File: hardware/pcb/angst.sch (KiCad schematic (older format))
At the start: 1 part

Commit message: Finish work on MCU block, start work on driver block
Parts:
- removed U?: STM32F303RBTx, Package_QFP:LQFP-64_10x10mm_P0.5mm, symbol MCU_ST_STM32F3:STM32F303RBTx
- added C? (x7): 100n, symbol Device:C_Small
- added D?: LED, symbol Device:LED
- added L?: INDUCTOR, symbol pspice:INDUCTOR
- added R?: 100k, symbol Device:R
- added R? (x3): 4k7, symbol Device:R
- added R?: 10k, symbol Device:R
- added R?: 22, symbol Device:R
- added R?: 560, symbol Device:R
- added SW?: SW_Push, symbol Switch:SW_Push
- added U?: STM32F303RETx, Package_QFP:LQFP-64_10x10mm_P0.5mm, symbol MCU_ST_STM32F3:STM32F303RETx
- added U?: M24C02-RDW, Package_SO:TSSOP-8_4.4x3mm_P0.65mm, symbol Memory_EEPROM:M24C02-RDW
- added Y?: Crystal_GND24, symbol Device:Crystal_GND24
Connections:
- net labels added: +3V3, GND, GNDA, PA0, PA1, PA10, PA11, PA12, PA13, PA14, PA15, PA2, PA3, PA4, PA5, PA6, PA7, PA8, PA9, PB0, PB1, PB10, PB11, PB12, PB13, PB14, PB2, PB3, PB4, PB5, PB6, PB7, PB8, PB9, PC0, PC1, PC10, PC11, PC12, PC13, PC14, PC15, PC2, PC3, PC4, PC5, PC7, PC8, PC9, PD2, nRST, pC6
- wire segments 0 -> 140
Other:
- note added: "EEPROM"
- note added: "uC - STM32F303"

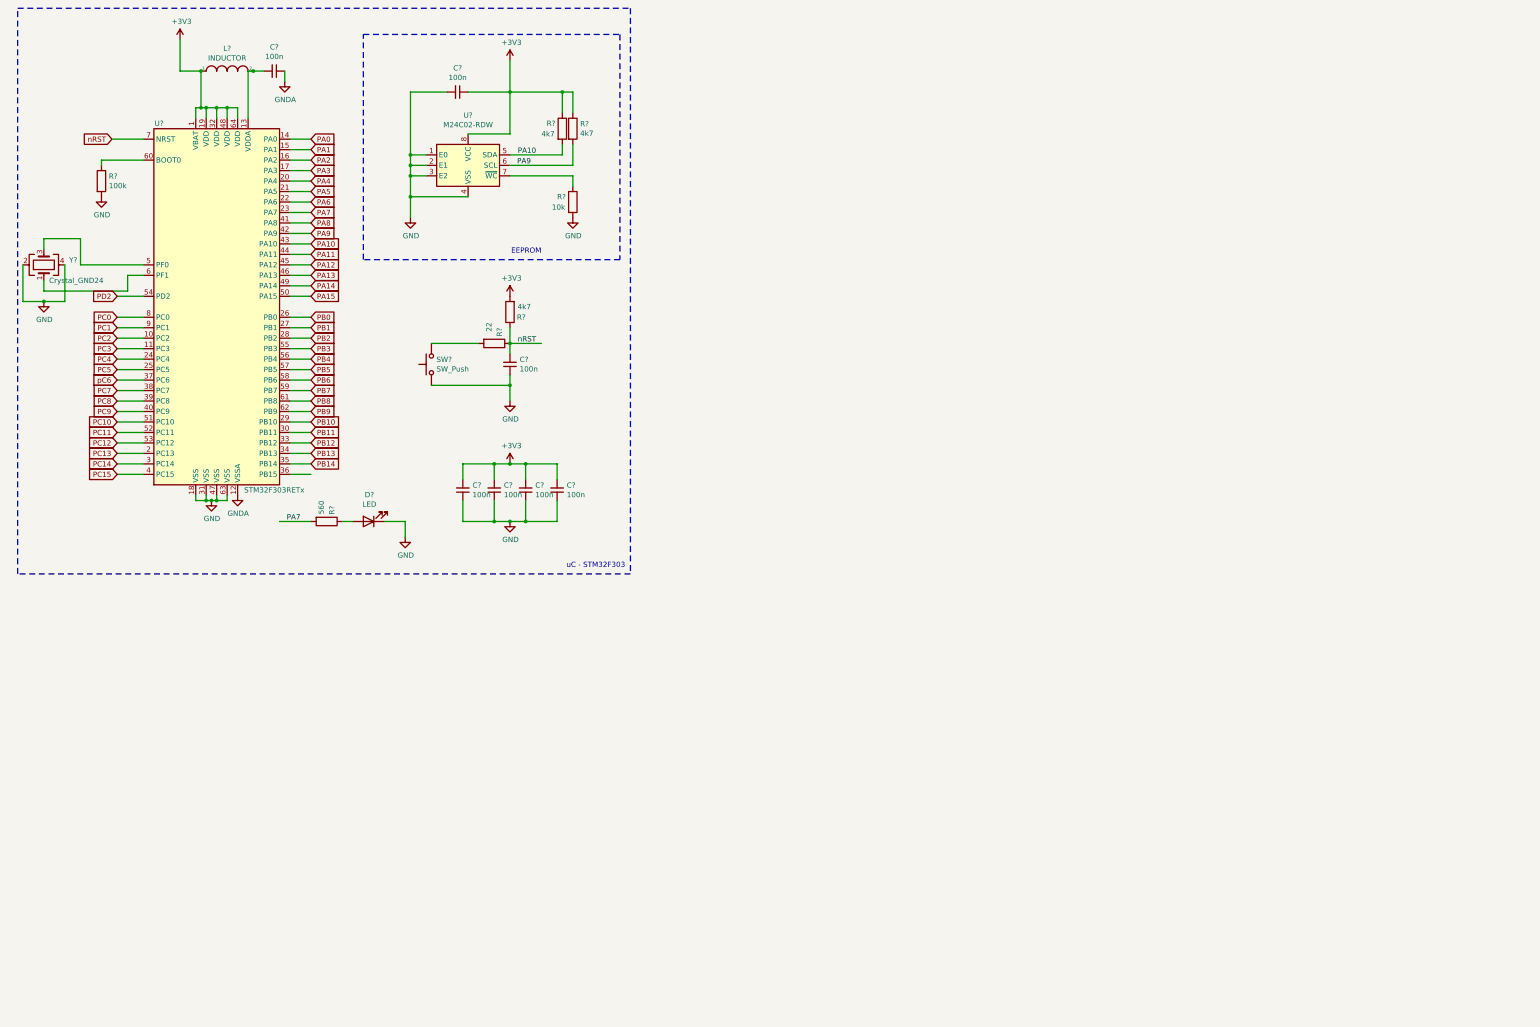
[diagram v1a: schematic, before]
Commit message: Add motor driver block and connector block.
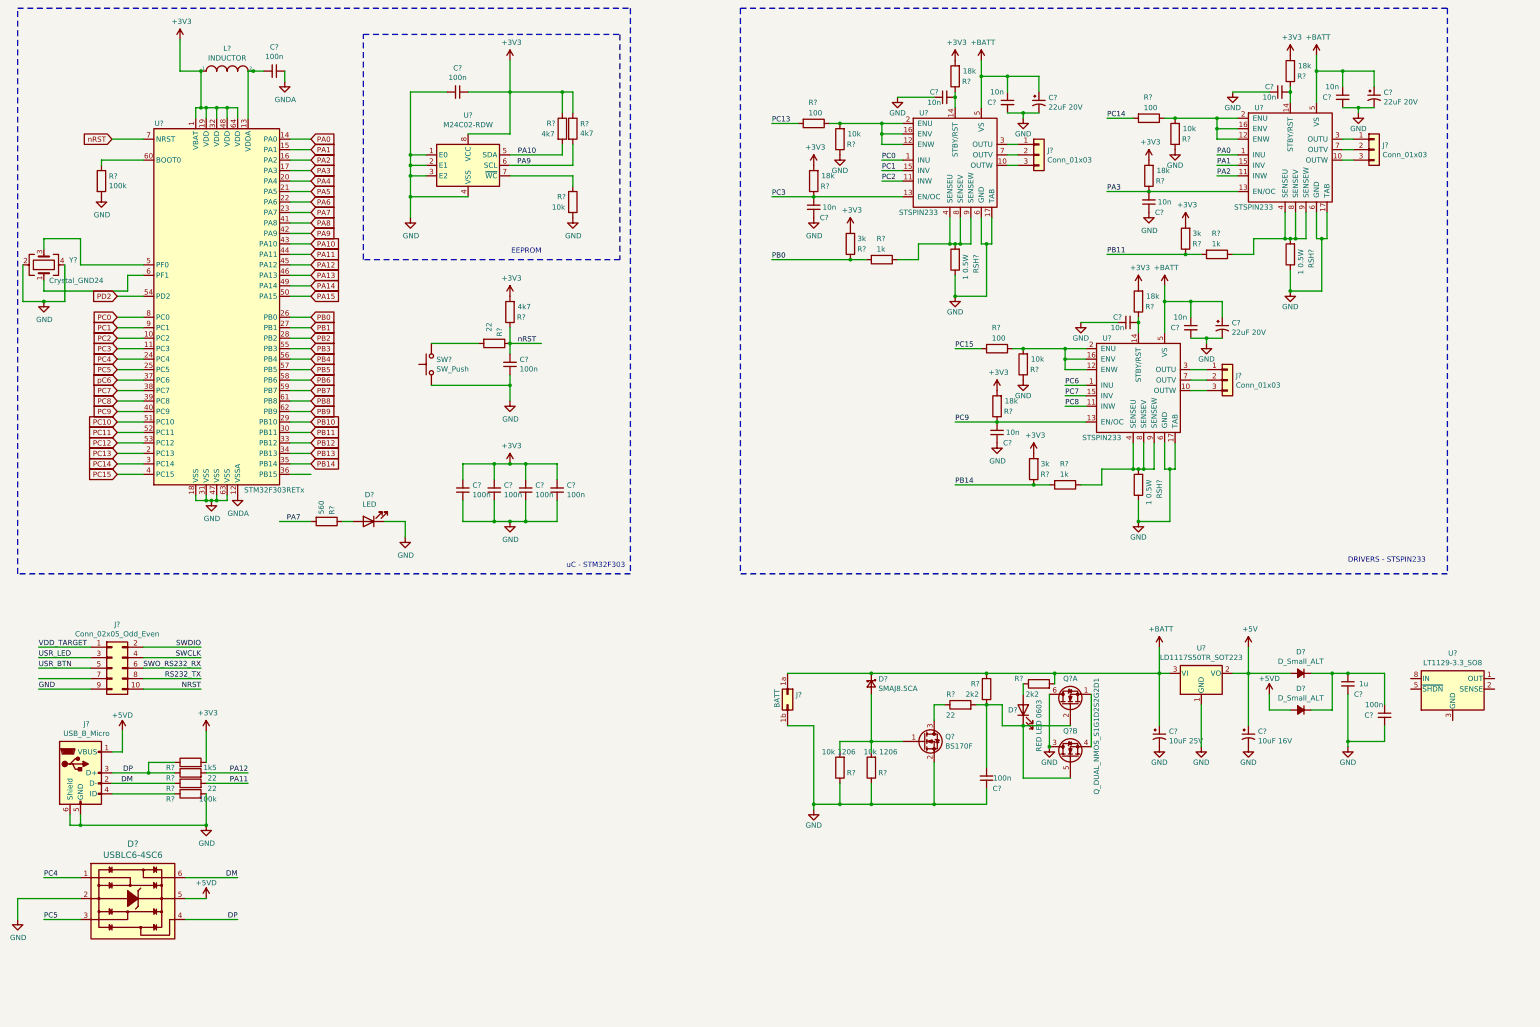
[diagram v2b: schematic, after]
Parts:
- added C? (x9): 10n, symbol Device:C_Small
- added C? (x3): 22uF 20V, symbol Device:CP1_Small
- added C? (x2): 100n, symbol Device:C_Small
- added C?: 10uF 25V, symbol Device:CP1_Small
- added C?: 10uF 16V, symbol Device:CP1_Small
- added C?: 1u, symbol Device:C_Small
- added D?: SMAJ8.5CA, symbol Device:D_Schottky_Small
- added D?: RED LED 0603, symbol Device:LED
- added D? (x2): D_Small_ALT, symbol Device:D_Small_ALT
- added D?: USBLC6-4SC6, digikey-footprints:SOT23-6L, symbol dk_TVS-Diodes:USBLC6-4SC6
- added J? (x3): Conn_01x03, symbol Connector_Generic:Conn_01x03
- added J?: Conn_02x05_Odd_Even, symbol Connector_Generic:Conn_02x05_Odd_Even
- added J?: BATT, symbol Connector_Generic:Conn_02x01_Row_Letter_Last
- added J?: USB_B_Micro, symbol Connector:USB_B_Micro
- added Q?: BS170F, Package_TO_SOT_SMD:SOT-23, symbol Transistor_FET:BS170F
- added Q? (x2): Q_DUAL_NMOS_S1G1D2S2G2D1, symbol Device:Q_DUAL_NMOS_S1G1D2S2G2D1
- added R? (x3): 100, symbol Device:R
- added R? (x3): 10k, symbol Device:R
- added R? (x6): 18k, symbol Device:R
- added R? (x3): 1k, symbol Device:R
- added R? (x3): 3k, symbol Device:R
- added R? (x2): 10k 1206, Resistor_SMD:R_1206_3216Metric_Pad1.42x1.75mm_HandSolder, symbol Device:R
- added R? (x3): 22, symbol Device:R
- added R? (x2): 2k2, symbol Device:R
- added R?: 100k, symbol Device:R
- added R?: 1k5, symbol Device:R
- added RSH? (x3): 1 0.5W, symbol Device:R
- added U? (x3): STSPIN233, symbol angst:STSPIN233
- added U?: LD1117S50TR_SOT223, Package_TO_SOT_SMD:SOT-223-3_TabPin2, symbol Regulator_Linear:LD1117S50TR_SOT223
- added U?: LT1129-3.3_SO8, Package_SO:SOIC-8_3.9x4.9mm_P1.27mm, symbol Regulator_Linear:LT1129-3.3_SO8
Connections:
- net +3V3: now also R?.2, R?.2, R?.2, R?.2, R?.2, R?.2, R?.2, R?.2, R?.2, R?.2
- net GND: now also C?.1, C?.1, C?.1, C?.1, C?.1, C?.1, C?.1, C?.2, C?.2, C?.2, C?.2, C?.2, C?.2, C?.2, C?.2, C?.2, C?.2, D?.2, J?.1b (Pin_1b), J?.5 (GND), J?.6 (Shield), J?.9 (Pin_9), Q?.2 (S), Q?.3 (D), Q?.6 (D), R?.1, R?.1, R?.1, R?.1, R?.1, R?.2, RSH?.1, RSH?.1, RSH?.1, U?.1 (GND), U?.17 (TAB), U?.17 (TAB), U?.17 (TAB), U?.6 (GND), U?.6 (GND), U?.6 (GND)
- net PA0: now also U?.1 (INU)
- net PA1: now also U?.15 (INV)
- net PA11: now also R?.2
- net PA12: now also R?.2
- net PA2: now also U?.11 (INW)
- net PA3: now also C?.2, R?.1, U?.13 (EN/OC)
- net PB0: now also R?.1, R?.2
- net PB11: now also R?.1, R?.2
- net PB14: now also R?.1, R?.2
- net PC0: now also U?.1 (INU)
- net PC1: now also U?.15 (INV)
- net PC13: now also R?.2
- net PC14: now also R?.2
- net PC15: now also R?.2
- net PC2: now also U?.11 (INW)
- net PC3: now also C?.2, R?.1, U?.13 (EN/OC)
- net PC4: now also D?.1
- net PC5: now also D?.3
- net PC7: now also U?.15 (INV)
- net PC8: now also U?.11 (INW)
- net PC9: now also C?.2, R?.1, U?.13 (EN/OC)
- new net: J?.3 (Pin_3), U?.10 (OUTW) (x3)
- new net: R?.1, R?.2, U?.12 (ENW), U?.16 (ENV), U?.2 (ENU) (x3)
- new net: C?.2, R?.1, U?.14 (STBY/RST) (x3)
- new net: J?.1 (Pin_1), U?.3 (OUTU) (x3)
- new net: R?.1, RSH?.2, U?.4 (SENSEU), U?.8 (SENSEV), U?.9 (SENSEW) (x3)
- new net: J?.2 (Pin_2), U?.7 (OUTV) (x3)
- new net: D?.2 (A), Q?.1 (G), R?.2, R?.2
- new net: Q?.3 (D), R?.1
- new net: C?.2, D?.1 (K), Q?.2 (G), Q?.5 (G), R?.2, R?.2
- new net: Q?.1 (S), Q?.4 (S)
- new net: D?.2 (A), R?.1
- new net: C?.1, C?.1, D?.1 (K), D?.1 (K)
- new net: U?.3 (GND), U?.6 (GND), U?.7 (GND)
- new net: J?.4 (ID), R?.1
- new net +5V: C?.1, D?.2 (A), U?.2 (VO)
- new net +5VD: D?.2 (A), D?.5, J?.1 (VBUS)
- new net +BATT: C?.1, C?.1, C?.1, C?.1, C?.1, C?.1, C?.1, D?.1 (K), J?.1a (Pin_1a), R?.1, R?.2, U?.3 (VI), U?.5 (VS), U?.5 (VS), U?.5 (VS)
- new net DM: D?.6, J?.2 (D-), R?.1
- new net DP: D?.4, J?.3 (D+), R?.1, R?.1
- new net NRST: J?.10 (Pin_10)
- new net PC6: U?.1 (INU)
- new net RS232_TX: J?.8 (Pin_8)
- new net SWCLK: J?.4 (Pin_4)
- new net SWDIO: J?.2 (Pin_2)
- new net SWO_RS232_RX: J?.6 (Pin_6)
- new net USR_BTN: J?.5 (Pin_5)
- new net USR_LED: J?.3 (Pin_3)
- new net VDD_TARGET: J?.1 (Pin_1)
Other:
- note added: "DRIVERS - STSPIN233\n"

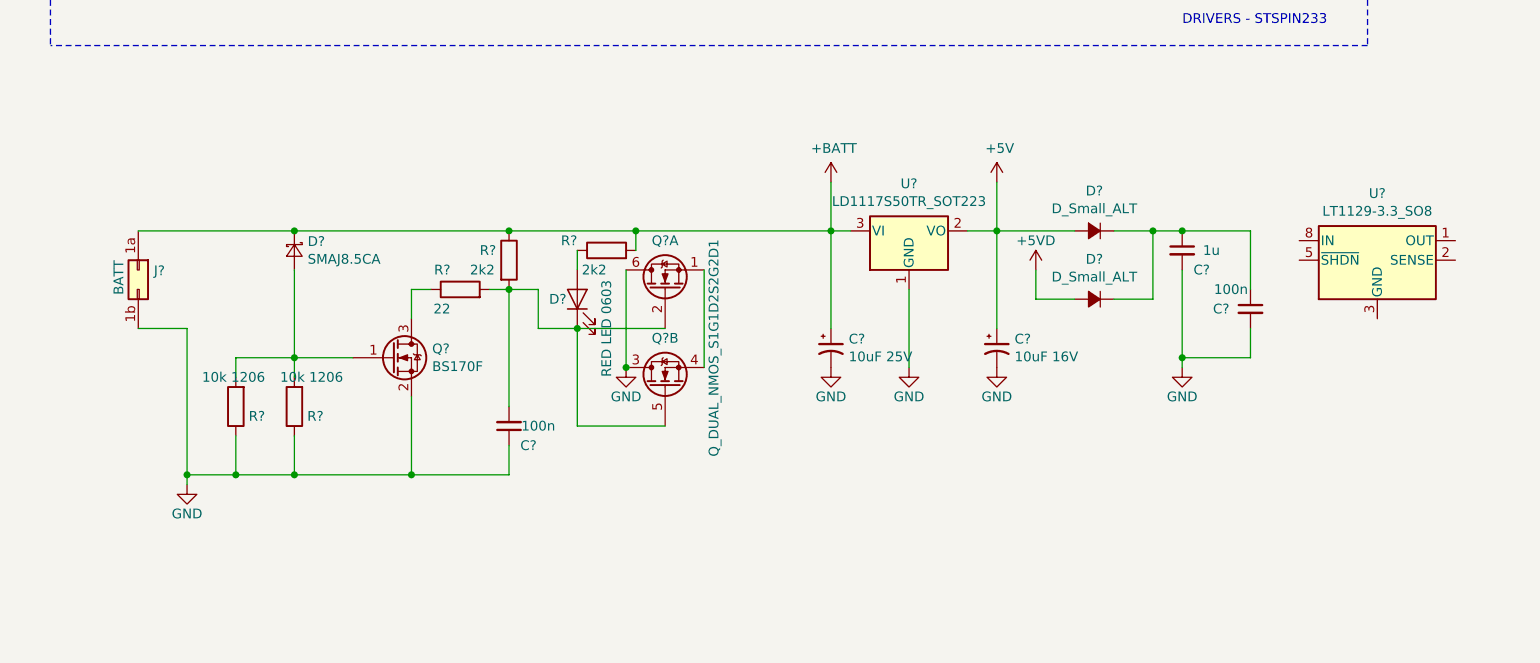
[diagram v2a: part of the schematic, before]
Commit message: Add power block
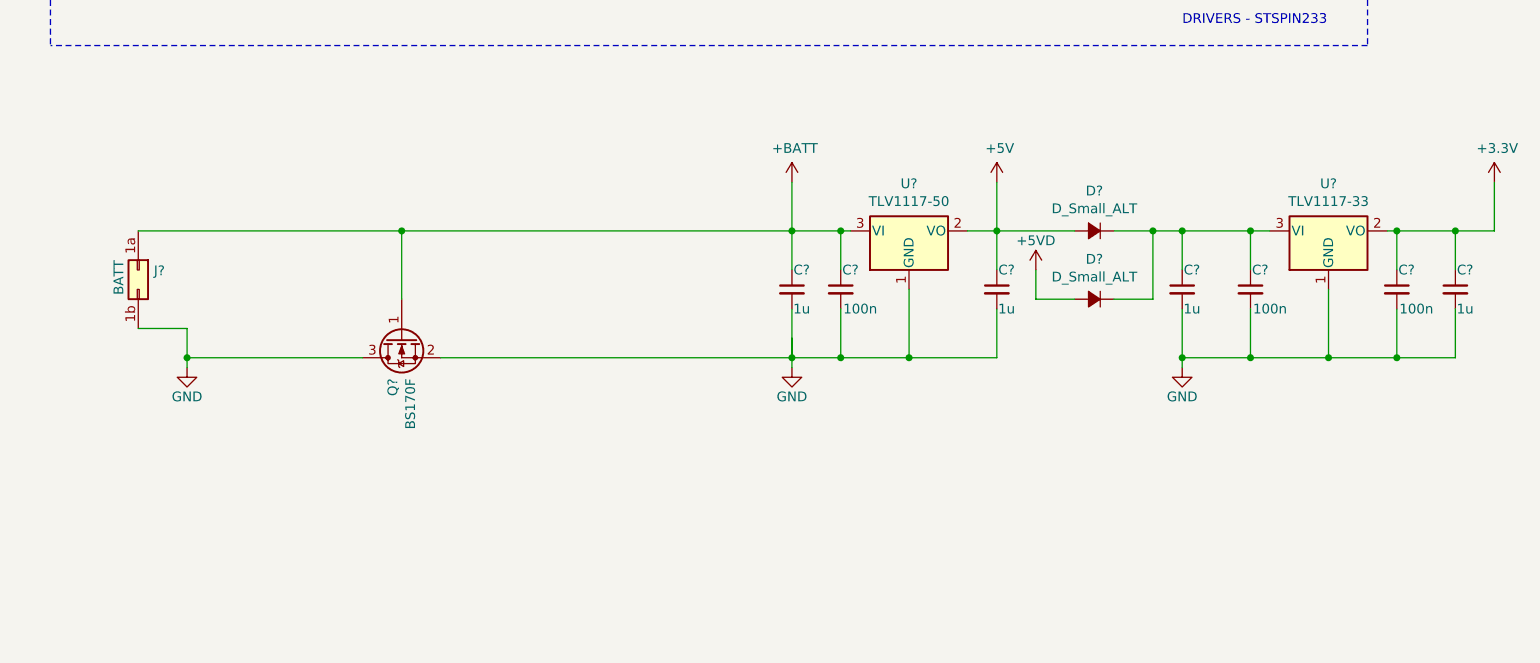
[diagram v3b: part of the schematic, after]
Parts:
- removed C?: 100n, symbol Device:C_Small
- removed C?: 10uF 25V, symbol Device:CP1_Small
- removed C?: 10uF 16V, symbol Device:CP1_Small
- removed D?: SMAJ8.5CA, symbol Device:D_Schottky_Small
- removed D?: RED LED 0603, symbol Device:LED
- removed Q? (x2): Q_DUAL_NMOS_S1G1D2S2G2D1, symbol Device:Q_DUAL_NMOS_S1G1D2S2G2D1
- removed R? (x2): 10k 1206, Resistor_SMD:R_1206_3216Metric_Pad1.42x1.75mm_HandSolder, symbol Device:R
- removed R?: 22, symbol Device:R
- removed R? (x2): 2k2, symbol Device:R
- removed U?: LD1117S50TR_SOT223, Package_TO_SOT_SMD:SOT-223-3_TabPin2, symbol Regulator_Linear:LD1117S50TR_SOT223
- removed U?: LT1129-3.3_SO8, Package_SO:SOIC-8_3.9x4.9mm_P1.27mm, symbol Regulator_Linear:LT1129-3.3_SO8
- added C? (x3): 1u, symbol Device:C_Small
- added C? (x2): 100n, symbol Device:C_Small
- added U?: TLV1117-33, symbol Regulator_Linear:TLV1117-33
- added U?: TLV1117-50, symbol Regulator_Linear:TLV1117-50
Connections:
- net +3V3: now also C?.1, C?.1, U?.2 (VO)
- net +5V: now also C?.1, U?.2 (VO)
- net +BATT: now also Q?.1 (G), C?.1, C?.1, U?.3 (VI)
- net GND: now also Q?.3 (D), C?.2, C?.2, C?.2, C?.2, C?.2, U?.1 (GND), U?.1 (GND)
- net at C?.1, C?.1, D?.1 (K)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: now also U?.3 (VI)
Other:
- moved on the sheet: C?, Q?

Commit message: Clean up power concept. Add connector block
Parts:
- removed D?: D_Small_ALT, symbol Device:D_Small_ALT
- removed Q?: BS170F, Package_TO_SOT_SMD:SOT-23, symbol Transistor_FET:BS170F
- added D3: SMAJ8.5CALFCT-ND, Diode_SMD:D_SMA, symbol Device:D_ALT
- added D4: STPS2L30, Diode_SMD:D_SMA, symbol Device:D_Small_ALT
- added J? (x2): Conn_01x02_Male, symbol Connector:Conn_01x02_Male
- added J?: Conn_01x04_Male, symbol Connector:Conn_01x04_Male
- added Q1: IRLML6401TRPBF, digikey-footprints:SOT-23-3, symbol dk_Transistors-FETs-MOSFETs-Single:IRLML6401TRPBF
- added R22: 2k2, Resistor_SMD:R_0603_1608Metric_Pad1.05x0.95mm_HandSolder, symbol Device:R
- added R? (x2): 47k, Resistor_SMD:R_0603_1608Metric_Pad1.05x0.95mm_HandSolder, symbol Device:R
- C1, C10, C11, C13, C14, C15, C16, C17, C19, C2, C20, C21, C22, C24, C25, C26, C3, C4, C5, C6, C7, C8, C9: renamed from C?; footprint (none) -> Capacitor_SMD:C_0603_1608Metric_Pad1.05x0.95mm_HandSolder
- C12, C18, C23: renamed from C?; footprint (none) -> Capacitor_Tantalum_SMD:CP_EIA-1608-08_AVX-J_Pad1.25x1.05mm_HandSolder
- D2: renamed from D?; footprint (none) -> LED_SMD:LED_0603_1608Metric_Pad1.05x0.95mm_HandSolder
- D5: renamed from D?; value D_Small_ALT -> STPS2L30; footprint (none) -> Diode_SMD:D_SMA
- J1: renamed from J?; footprint (none) -> Connector_USB:USB_Micro-B_Molex-105017-0001
- R1, R10, R11, R12, R13, R14, R15, R16, R17, R18, R19, R2, R20, R21, R23, R24, R25, R26, R27, R28, R29, R3, R30, R4, R5, R6, R7, R8, R9: renamed from R?; footprint (none) -> Resistor_SMD:R_0603_1608Metric_Pad1.05x0.95mm_HandSolder
- RSH1, RSH2, RSH3: renamed from RSH?; footprint (none) -> Resistor_SMD:R_1206_3216Metric_Pad1.42x1.75mm_HandSolder
- SW1: renamed from SW?; footprint (none) -> Button_Switch_SMD:SW_SPST_EVPBF
- U3, U4, U6: renamed from U?; footprint (none) -> digikey-footprints:VFQFN-16-1EP_3x3mm
- U5, U7: renamed from U?; footprint (none) -> digikey-footprints:SOT-223
- Y1: renamed from Y?; footprint (none) -> Crystal:Crystal_SMD_0603-4Pin_6.0x3.5mm_HandSoldering
- gave numbers to parts that had none: 9
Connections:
- net GNDA is gone; now on net GND: C1.1, U1.12 (VSSA)
- net NRST is gone; now on net nRST: J2.10 (Pin_10)
- net RS232_TX is gone; now on net PC4: J2.8 (Pin_8)
- net SWCLK is gone; now on net PA14: J2.4 (Pin_4)
- net SWDIO is gone; now on net PA13: J2.2 (Pin_2)
- net SWO_RS232_RX is gone; now on net PC5: J2.6 (Pin_6)
- net VDD_TARGET is gone; now on net +3V3: J2.1 (Pin_1)
- net pC6 is gone; now on net PC6: U1.37 (PC6)
- net +5V: now also D4.2 (A)
- net +BATT: now also D3.1 (K), Q1.2 (S); no longer J3.1a (Pin_1a)
- net GND: now also R22.1, R?.1, R?.1
- net PA4: now also J?.1 (Pin_1)
- net PA5: now also J?.2 (Pin_2)
- net PA6: now also J?.3 (Pin_3)
- net PA7: now also J?.4 (Pin_4); no longer R6.2
- net PA8: now also R6.2
- net PB3: now also J?.1 (Pin_1)
- net PB4: now also J?.2 (Pin_2)
- net PB6: now also J?.1 (Pin_1)
- net PB7: now also J?.2 (Pin_2)
- net PC4: now also R?.2
- net PC5: now also R?.2
- net PB15: now reaches U1.36 (PB15)
- net at C22.1, C24.1, D5.1 (K)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: now also D4.1 (K)
- net USR_BTN: no longer names the net of J2.5 (Pin_5)
- net USR_LED: no longer names the net of J2.3 (Pin_3)
- new net: D3.2 (A), Q1.1 (G), R22.2
- new net: J3.1a (Pin_1a), Q1.3 (D)
- no-connect marks 0 -> 3
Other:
- note added: "Connector"
- note added: "I2C1_SCL"
- note added: "I2C1_SDA\n"
- note added: "IMU\n"
- note added: "Power"
- note added: "RS232_TX\n"
- note added: "SPI1"
- note added: "SPI1_MISO"
- note added: "SPI1_MOSI"
- note added: "SPI1_NSS"
- note added: "SPI1_SCK"
- note added: "SWCLK"
- note added: "SWDIO\n"
- note added: "SWO_RS232_RX"
- note added: "USART2"
- note added: "USART2_RX"
- note added: "USART2_TX\n"
- note added: "nRST"
- moved on the sheet: C14, C16, C19, C22, C24, C25, C26, D1, D5, J3, U5, U7
